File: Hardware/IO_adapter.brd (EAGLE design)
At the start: 67.3 x 41.9 mm, 23 parts, among them Y1 32Khz

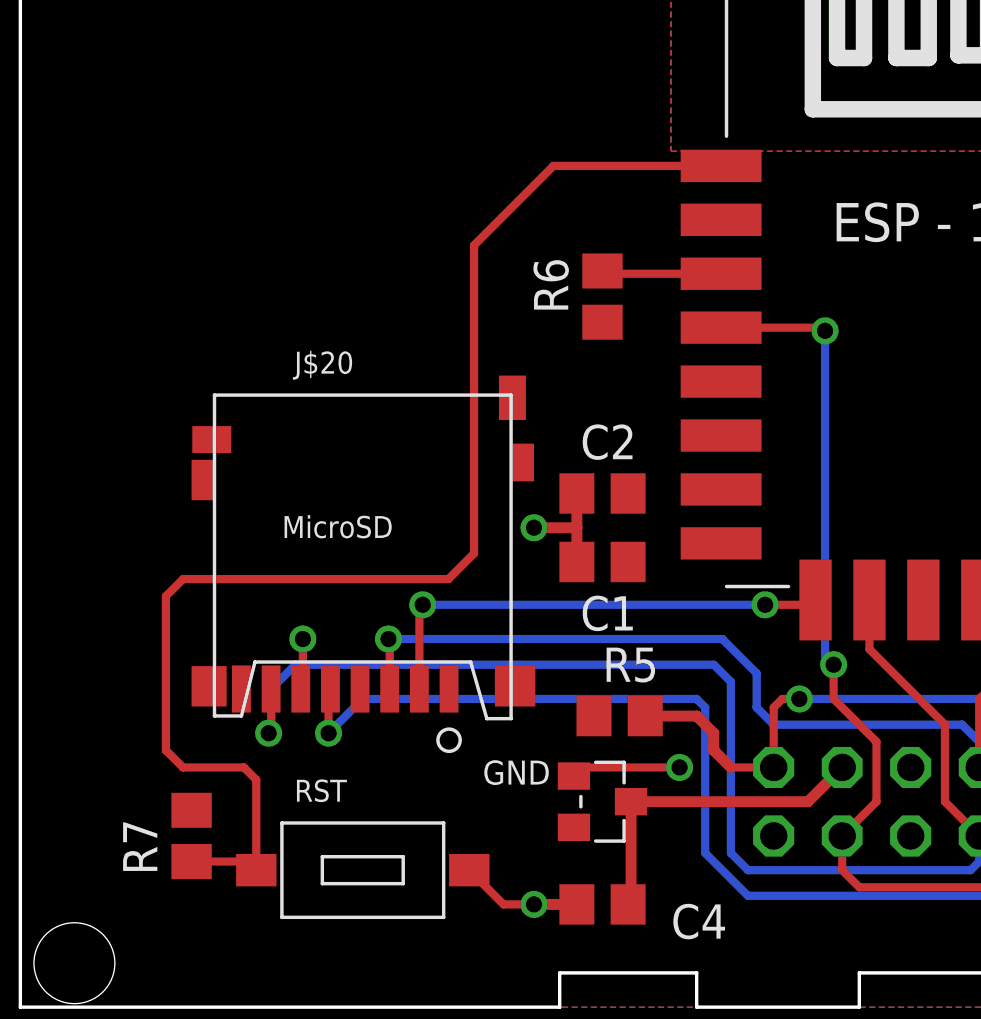
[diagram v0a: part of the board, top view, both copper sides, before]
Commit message: corrected sd card orientation
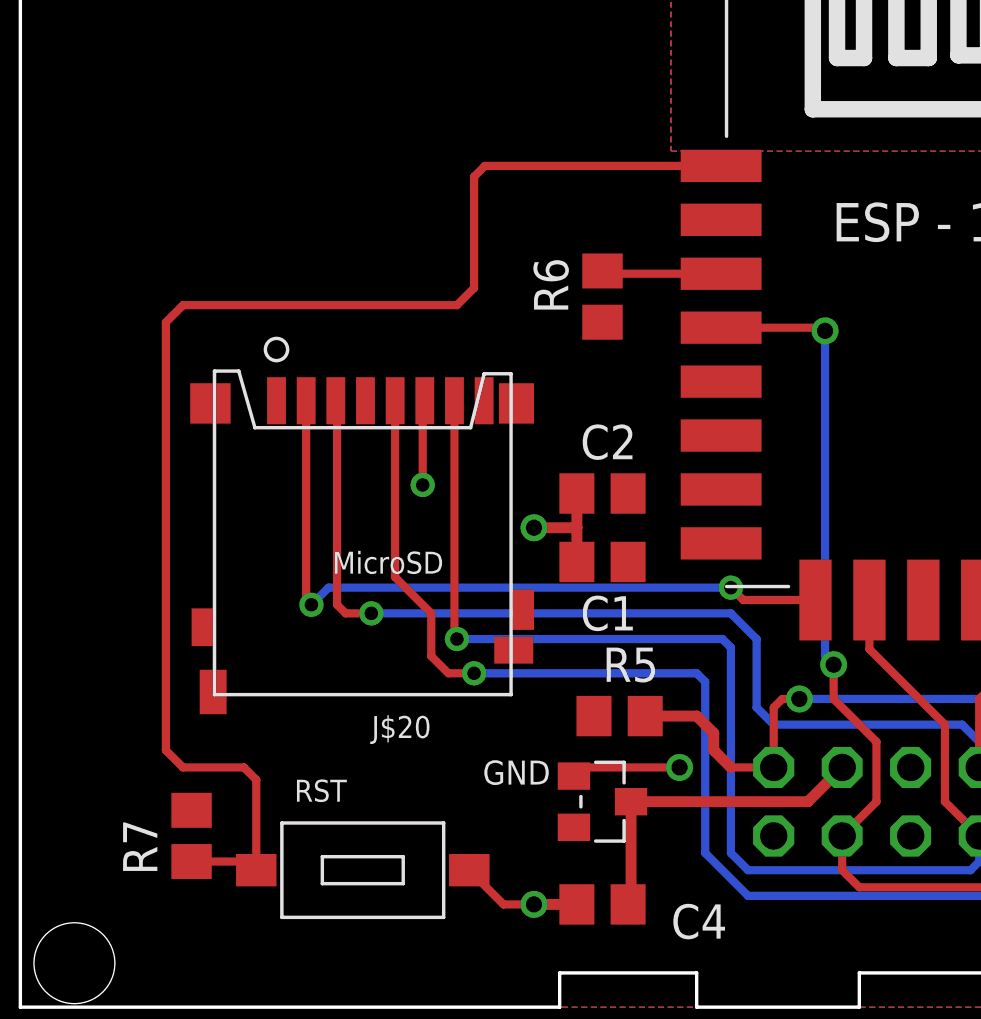
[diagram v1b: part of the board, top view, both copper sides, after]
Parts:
- moved J$20 8.89 mm to (12.7, 21.6), turned to 180 degrees
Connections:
- net GND: now also U$1.P-
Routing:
- net CSSD: track 17.8 -> 26.8 mm
- net MOSI: track 34.1 -> 43.0 mm
- net SCLK: track 45.9 -> 51.1 mm
- net RST: track 49.3 -> 51.0 mm
- net GND: track 36.8 -> 37.9 mm
- net MISO: track 48.5 -> 47.8 mm

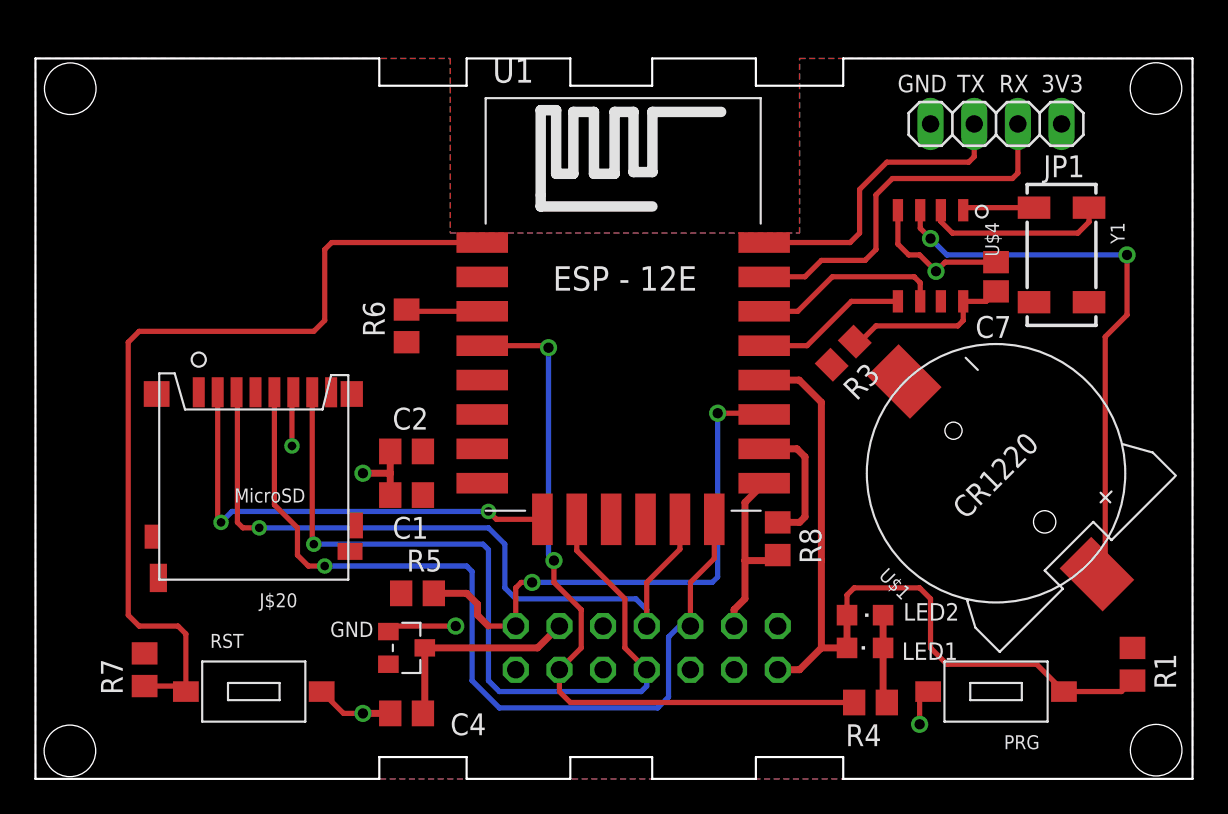
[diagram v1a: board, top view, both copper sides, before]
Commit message: corrected a major mistake
I had connected MOSI/MISO/SCLK to the primary hw SPI - now they are correctly conntected to the secondary bus.
MOSI->HSPI-D(GPIO13)
MISO->HSPI-Q(GPIO12)
SCLK->HSPI-CLK(GPIO14)
CSSD->HSPI-CD(GPIO15)

also added some minor changes to better fit the case
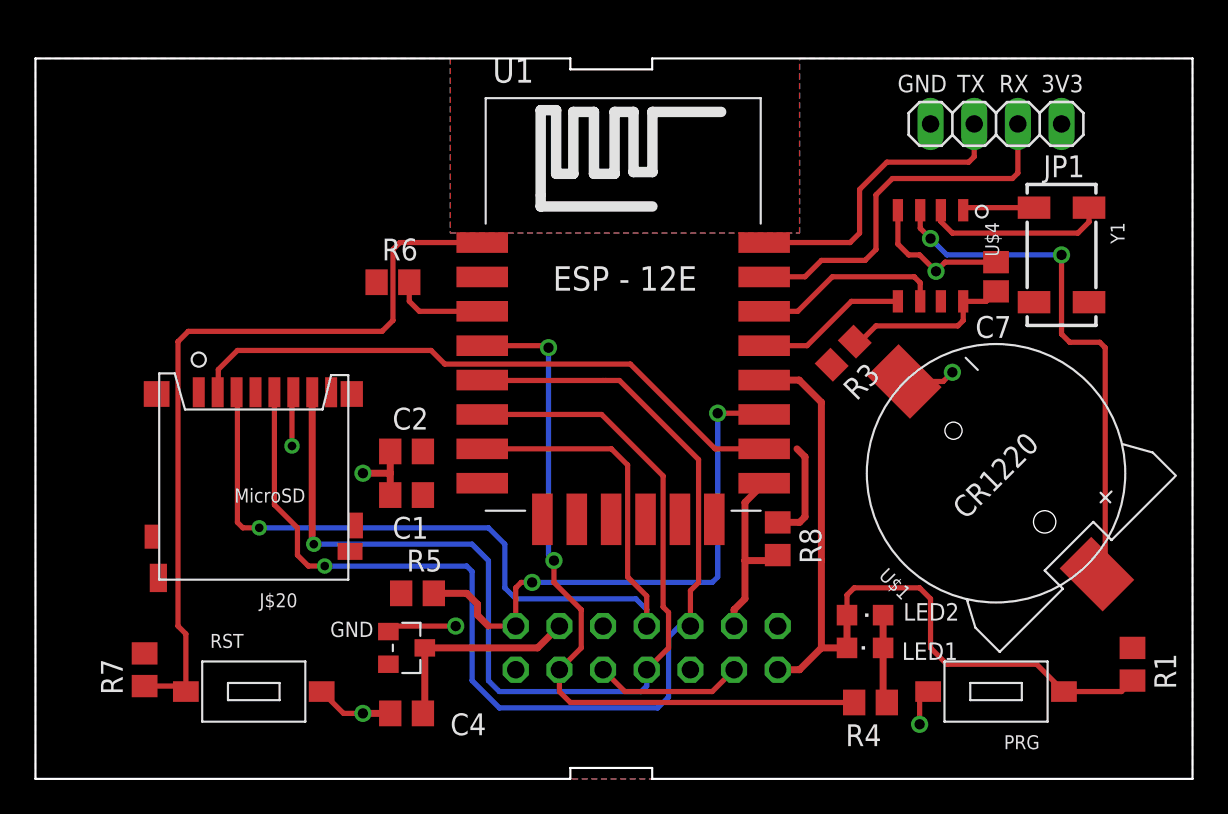
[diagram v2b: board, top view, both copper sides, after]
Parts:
- moved R6 2.66 mm to (20.8, 28.9), turned to 0 degrees
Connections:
- removed net CSSD: J$20.P$2, U1.CS0
- removed net GPIO10: U1.GPIO10
- removed net GPIO12: U1.GPIO12
- removed net GPIO13: U1.GPIO13
- removed net GPIO14: U1.GPIO14
- removed net GPIO9: U1.GPIO9
- removed net MISO: J$20.P$7, SV1.8, U1.MISO
- removed net MOSI: J$20.P$3, SV1.7, U1.MOSI
- removed net SCLK: J$20.P$5, SV1.9, U1.SCLK
- new net HCLK: J$20.P$5, SV1.9, U1.GPIO14
- new net HCSSD: J$20.P$2, U1.GPIO15
- new net HMISO: J$20.P$7, SV1.8, U1.GPIO12
- new net HMOSI: J$20.P$3, SV1.7, U1.GPIO13
- net GPIO15: no longer U1.GPIO15
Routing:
- net HCLK: track 0.00 -> 68.7 mm, vias 0 -> 1
- net HMISO: track 0.00 -> 60.9 mm, vias 0 -> 1
- net HMOSI: track 0.00 -> 54.6 mm, vias 0 -> 1
- net SCLK: track 51.1 -> 0.00 mm, vias 1 -> 0
- net MISO: track 47.8 -> 0.00 mm, vias 1 -> 0
- net MOSI: track 43.0 -> 0.00 mm, vias 1 -> 0
- net HCSSD: track 0.00 -> 35.9 mm
- net CSSD: track 26.8 -> 0.00 mm, vias 2 -> 0
- net GND: track 37.9 -> 49.6 mm, vias 6 -> 7
- net RST: track 51.0 -> 45.6 mm
- net VBATT: track 32.9 -> 30.7 mm
- net GPIO15: track 7.78 -> 5.87 mm
- net CH_PD: track 4.44 -> 5.59 mm
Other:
- outline, holes or cut-outs redrawn

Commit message: SPI termination resistor positions
added SPI termination resistor positions
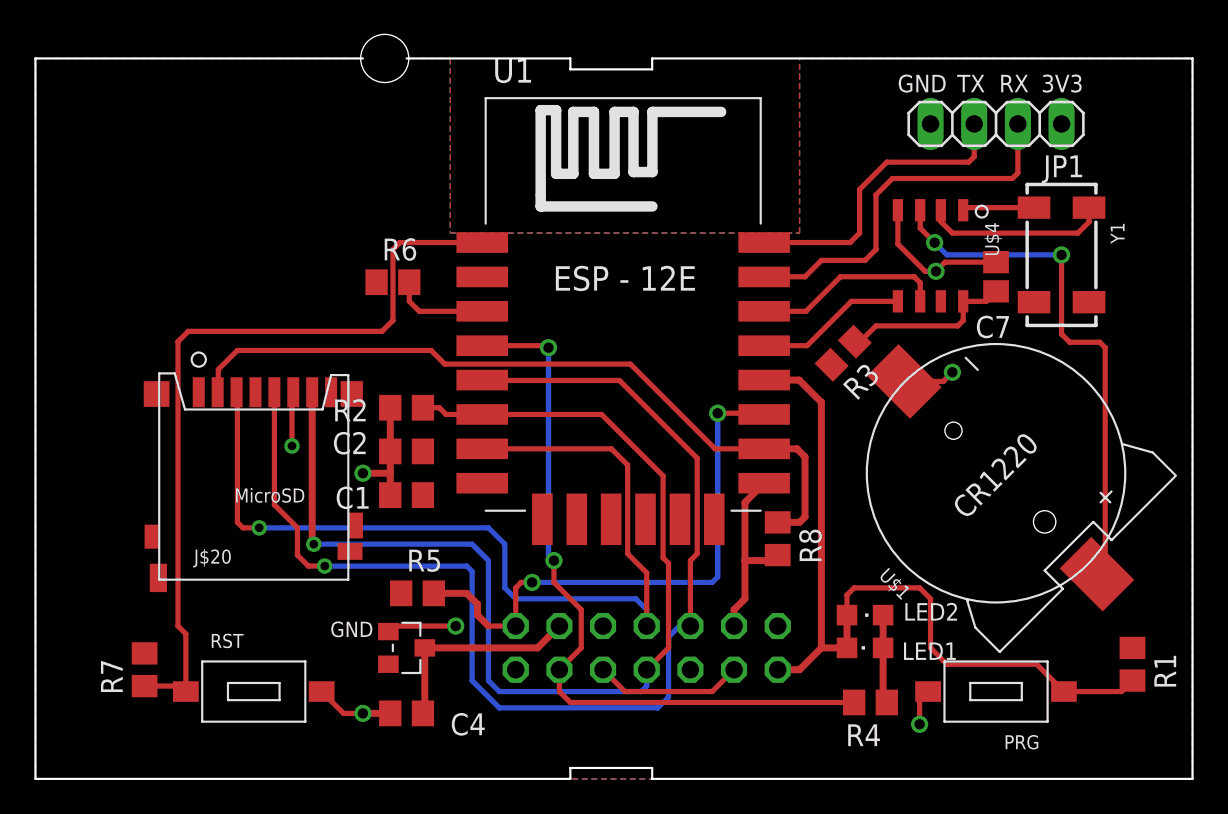
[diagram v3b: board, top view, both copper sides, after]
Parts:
- added R2: 330, resistor:R0805
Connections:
- removed net GPIO15: R8.2
- net GND: now also R2.2
- net HCSSD: now also R8.2
- net HMISO: now also R2.1
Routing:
- net HCSSD: track 35.9 -> 43.7 mm
- net GPIO15: track 5.87 -> 0.00 mm
- net HMISO: track 60.9 -> 64.5 mm
- net GND: track 49.6 -> 52.1 mm
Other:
- outline, holes or cut-outs redrawn

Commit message: mechanical fitting
moved the clamp positions such that they should fit unmodified.
Added silkscreen signal names for the power board ribbon connector, improved 3V3 connection on IO Board
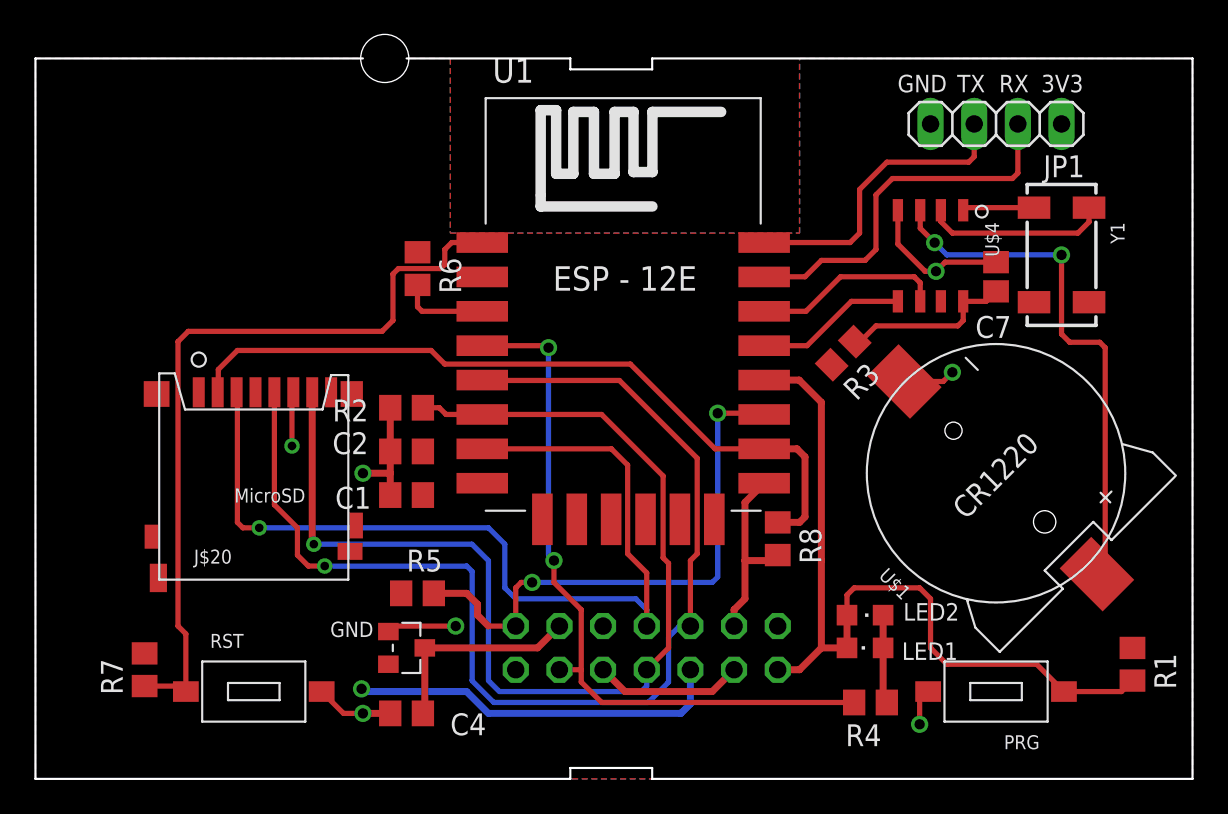
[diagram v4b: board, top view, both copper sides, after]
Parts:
- moved R6 1.63 mm to (22.2, 29.7), turned to 270 degrees
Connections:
- net 3V3: now also SV1.10
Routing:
- net 3V3: track 0.00 -> 21.9 mm, vias 0 -> 1
- net GPIO16: track 42.6 -> 41.8 mm
- net HCLK: track 68.6 -> 67.9 mm
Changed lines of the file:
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@@
 <attribute name="NAME" x="21.59" y="12.065" size="1.27" layer="25"/>
 </element>
-<element name="R6" library="resistor" package="R0805" value="10K" x="20.79625" y="28.8925" smashed="yes">
-<attribute name="NAME" x="20.16125" y="30.1625" size="1.27" layer="25"/>
+<element name="R6" library="resistor" package="R0805" value="10K" x="22.225" y="29.68625" smashed="yes" rot="R270">
+<attribute name="NAME" x="23.495" y="30.32125" size="1.27" layer="25" rot="R270"/>
 </element>
 <element name="R7" library="resistor" package="R0805" value="10K" x="6.35" y="6.35" smashed="yes" rot="R270">
@@
 <wire x1="14.9225" y1="22.4125" x2="15" y2="22.49" width="0.3048" layer="1"/>
 <contactref element="U$1" pad="P-"/>
-<wire x1="33.02" y1="6.35" x2="34.29" y2="5.08" width="0.3048" layer="1"/>
-<wire x1="34.29" y1="5.08" x2="39.37" y2="5.08" width="0.3048" layer="1"/>
-<wire x1="39.37" y1="5.08" x2="40.64" y2="6.35" width="0.3048" layer="1"/>
 <via x="53.34" y="23.65375" extent="1-16" drill="0.6"/>
 <wire x1="50.54134375" y1="23.118653125" x2="52.804903125" y2="23.118653125" width="0.3048" layer="1"/>
@@
 <wire x1="50.17" y1="31.11" x2="51.7525" y2="29.5275" width="0.3048" layer="1"/>
 <wire x1="51.7525" y1="29.5275" x2="52.3875" y2="29.5275" width="0.3048" layer="1"/>
+<wire x1="33.02" y1="6.35" x2="34.29" y2="5.08" width="0.4064" layer="1"/>
+<wire x1="34.29" y1="5.08" x2="39.37" y2="5.08" width="0.4064" layer="1"/>
+<wire x1="39.37" y1="5.08" x2="40.64" y2="6.35" width="0.4064" layer="1"/>
 </signal>
 <signal name="3V3">
@@
 </polygon>
 <contactref element="JP1" pad="1"/>
+<contactref element="SV1" pad="10"/>
+<via x="18.970625" y="5.23875" extent="1-16" drill="0.6" shape="octagon"/>
+<wire x1="26.3525" y1="3.81" x2="37.544375" y2="3.81" width="0.4064" layer="16"/>
+<wire x1="37.544375" y1="3.81" x2="38.1" y2="4.365625" width="0.4064" layer="16"/>
+<wire x1="38.1" y1="4.365625" x2="38.1" y2="6.35" width="0.4064" layer="16"/>
+<wire x1="18.970625" y1="5.23875" x2="19.129375" y2="5.08" width="0.4064" layer="16"/>
+<wire x1="19.129375" y1="5.08" x2="25.0825" y2="5.08" width="0.4064" layer="16"/>
+<wire x1="25.0825" y1="5.08" x2="26.3525" y2="3.81" width="0.4064" layer="16"/>
 </signal>
 <signal name="ADCCS1">
@@
 <contactref element="SV1" pad="4"/>
 <contactref element="U1" pad="GPIO16"/>
-<wire x1="47.6275" y1="4.445" x2="31.115" y2="4.445" width="0.3048" layer="1"/>
-<wire x1="31.115" y1="4.445" x2="30.48" y2="5.08" width="0.3048" layer="1"/>
-<wire x1="30.48" y1="5.08" x2="30.48" y2="6.35" width="0.3048" layer="1"/>
-<wire x1="30.48" y1="6.35" x2="31.75" y2="7.62" width="0.3048" layer="1"/>
 <via x="30.1625" y="12.7" extent="1-16" drill="0.6" shape="octagon"/>
 <via x="29.845" y="25.0825" extent="1-16" drill="0.6" shape="octagon"/>
@@
 <wire x1="30.1625" y1="12.7" x2="29.845" y2="13.0175" width="0.3048" layer="16"/>
 <wire x1="29.845" y1="13.0175" x2="29.845" y2="25.0825" width="0.3048" layer="16"/>
-<wire x1="31.75" y1="7.62" x2="31.75" y2="9.8425" width="0.3048" layer="1"/>
+<wire x1="31.75" y1="5.635625" x2="31.75" y2="6.35" width="0.3048" layer="1"/>
+<wire x1="31.75" y1="6.35" x2="31.75" y2="9.8425" width="0.3048" layer="1"/>
 <wire x1="31.75" y1="9.8425" x2="30.1625" y2="11.43" width="0.3048" layer="1"/>
 <wire x1="30.1625" y1="11.43" x2="30.1625" y2="12.7" width="0.3048" layer="1"/>
+<wire x1="31.75" y1="5.635625" x2="32.940625" y2="4.445" width="0.3048" layer="1"/>
+<wire x1="32.940625" y1="4.445" x2="47.6275" y2="4.445" width="0.3048" layer="1"/>
+<wire x1="30.48" y1="6.35" x2="31.75" y2="6.35" width="0.3048" layer="1"/>
 </signal>
 <signal name="5V">
@@
 <contactref element="R7" pad="2"/>
 <contactref element="RST" pad="P$1"/>
-<wire x1="20.79625" y1="30.7975" x2="21.19875" y2="31.2" width="0.3048" layer="1"/>
-<wire x1="21.19875" y1="31.2" x2="25.99" y2="31.2" width="0.3048" layer="1"/>
 <wire x1="8.75" y1="5.08" x2="8.43" y2="5.4" width="0.3048" layer="1"/>
 <wire x1="8.43" y1="5.4" x2="6.35" y2="5.4" width="0.3048" layer="1"/>
 <wire x1="8.75" y1="8.4325" x2="8.75" y2="5.08" width="0.3048" layer="1"/>
-<wire x1="20.79625" y1="30.7975" x2="20.79625" y2="26.67" width="0.3048" layer="1"/>
-<wire x1="20.79625" y1="26.67" x2="20.16125" y2="26.035" width="0.3048" layer="1"/>
 <wire x1="20.16125" y1="26.035" x2="8.89" y2="26.035" width="0.3048" layer="1"/>
 <wire x1="8.2925" y1="8.89" x2="8.75" y2="8.4325" width="0.3048" layer="1"/>
 <wire x1="8.2925" y1="8.89" x2="8.2925" y2="25.4375" width="0.3048" layer="1"/>
 <wire x1="8.2925" y1="25.4375" x2="8.89" y2="26.035" width="0.3048" layer="1"/>
+<wire x1="25.99" y1="31.2" x2="24.215" y2="31.2" width="0.3048" layer="1"/>
+<wire x1="24.215" y1="31.2" x2="23.8125" y2="30.7975" width="0.3048" layer="1"/>
+<wire x1="23.8125" y1="30.7975" x2="23.8125" y2="29.924375" width="0.3048" layer="1"/>
+<wire x1="23.8125" y1="29.924375" x2="23.574375" y2="29.68625" width="0.3048" layer="1"/>
+<wire x1="23.574375" y1="29.68625" x2="21.11375" y2="29.68625" width="0.3048" layer="1"/>
+<wire x1="21.11375" y1="29.68625" x2="20.79625" y2="29.36875" width="0.3048" layer="1"/>
+<wire x1="20.79625" y1="29.36875" x2="20.79625" y2="26.67" width="0.3048" layer="1"/>
+<wire x1="20.79625" y1="26.67" x2="20.16125" y2="26.035" width="0.3048" layer="1"/>
 </signal>
 <signal name="ADC">
@@
 <contactref element="U1" pad="CH_PD"/>
 <contactref element="R6" pad="2"/>
-<wire x1="25.99" y1="27.2" x2="22.33" y2="27.2" width="0.3048" layer="1"/>
-<wire x1="22.33" y1="27.2" x2="21.74625" y2="27.78375" width="0.3048" layer="1"/>
-<wire x1="21.74625" y1="27.78375" x2="21.74625" y2="28.8925" width="0.3048" layer="1"/>
+<wire x1="25.99" y1="27.2" x2="22.48875" y2="27.2" width="0.3048" layer="1"/>
+<wire x1="22.48875" y1="27.2" x2="22.225" y2="27.46375" width="0.3048" layer="1"/>
+<wire x1="22.225" y1="27.46375" x2="22.225" y2="28.73625" width="0.3048" layer="1"/>
 </signal>
 <signal name="HCLK">
@@
 <contactref element="SV1" pad="9"/>
 <wire x1="25.4" y1="12.065" x2="25.4" y2="5.715" width="0.3048" layer="16"/>
-<wire x1="25.4" y1="5.715" x2="26.9875" y2="4.1275" width="0.3048" layer="16"/>
-<wire x1="26.9875" y1="4.1275" x2="36.195" y2="4.1275" width="0.3048" layer="16"/>
-<wire x1="36.195" y1="4.1275" x2="36.83" y2="4.7625" width="0.3048" layer="16"/>
-<wire x1="36.83" y1="4.7625" x2="36.83" y2="8.255" width="0.3048" layer="16"/>
 <wire x1="36.83" y1="8.255" x2="37.465" y2="8.89" width="0.3048" layer="16"/>
 <wire x1="37.465" y1="8.89" x2="38.1" y2="8.89" width="0.3048" layer="16"/>
@@
 <wire x1="26.0125" y1="23.1775" x2="25.99" y2="23.2" width="0.3048" layer="1"/>
 <wire x1="38.496875" y1="18.653125" x2="33.9725" y2="23.1775" width="0.3048" layer="1"/>
+<wire x1="25.4" y1="5.715" x2="26.67" y2="4.445" width="0.3048" layer="16"/>
+<wire x1="26.67" y1="4.445" x2="35.639375" y2="4.445" width="0.3048" layer="16"/>
+<wire x1="35.639375" y1="4.445" x2="36.83" y2="5.635625" width="0.3048" layer="16"/>
+<wire x1="36.83" y1="5.635625" x2="36.83" y2="8.255" width="0.3048" layer="16"/>
 </signal>
 <signal name="HMISO">
